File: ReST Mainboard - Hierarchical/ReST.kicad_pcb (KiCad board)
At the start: 2 copper layers, 100 x 100 mm, 164 parts, among them IC1 AT24C256, P1 CONN_01X02, P10 CONN_02X04, P11 CONN_01X04, P12 CONN_01X04, P13 CONN_01X04, P14 CONN_01X04, P15 USB_OTG, P16 CONN_02X05, P17 CONN_02X05, P18 CONN_02X05, P19 CONN_01X04, P2 CONN_01X03, P20 CONN_01X02, P21 CONN_01X04, P22 CONN_02X03, P23 CONN_02X03, P24 CONN_01X04, P25 CONN_02X03, P26 CONN_02X03, P27 CONN_02X06, P28 CONN_02X02, P29 CONN_01X02, P3 CONN_01X02, P30 CONN_01X02, P31 CONN_01X02, P32 CONN_02X02, P33 CONN_02X02, P34 CONN_02X02, P35 CONN_02X03, P36 CONN_02X03, P37 CONN_02X03, P38 CONN_02X03, P39 CONN_02X03, P4 CONN_01X03, P5 CONN_01X03, P6 CONN_01X03, P7 CONN_01X03, P8 CONN_01X03, P9 CONN_01X03, Q1 TBD, Q10 Q_AOT240L, Q11 Q_AOT240L, Q12 Q_AOT240L, Q2 TBD, Q3 TBD, Q4 TBD, Q7 Q_BSH105/IRLML2502, Q8 Q_BSH105/IRLML2502, Q9 Q_BSH105/IRLML2502, U10 USBLC6-2, U3 ACT4088, U4 SC4626, U9 STM32F1/STM32F4, X1 Crystal_Small

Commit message: removed copper and solder mask around screw holes
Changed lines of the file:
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@@
 (kicad_pcb (version 4) (host pcbnew 4.0.2-stable)
   (general
-    (links 0)
+    (links 456)
     (no_connects 0)
-    (area 18.45 61.641666 122.348 168.25)
+    (area 19.444999 65.444999 119.455001 165.455001)
     (thickness 1.6)
     (drawings 1437)
@@
   )
   (layers
-    (0 F.Cu signal hide)
-    (31 B.Cu signal hide)
+    (0 F.Cu signal)
+    (31 B.Cu signal)
     (32 B.Adhes user)
     (33 F.Adhes user)
@@
     (mod_text_size 0.75 0.75)
     (mod_text_width 0.1)
-    (pad_size 1.6 1.6)
-    (pad_drill 0)
+    (pad_size 3.2 3.2)
+    (pad_drill 3.2)
     (pad_to_mask_clearance 0)
     (aux_axis_origin 246.2 149.45)
     (grid_origin 104.45 160.45)
-    (visible_elements 7FFFFDFF)
+    (visible_elements 7FFFFFFF)
     (pcbplotparams
       (layerselection 0x010f0_80000001)
@@
     (add_net "/Stepper and Endstop/Z_2B")
   )
+  (module ReST-Library:1pin locked (layer F.Cu)
+    (at 114.45 70.45)
+    (descr "module 1 pin (ou trou mecanique de percage)")
+    (tags DEV)
+    (solder_mask_margin 1.3)
+    (clearance 1.3)
+    (fp_text reference REF** (at 0 -0.9) (layer F.Fab)
+      (effects (font (size 1 1) (thickness 0.15)))
+    )
+    (fp_text value 1pin (at 0 1.2) (layer F.Fab)
+      (effects (font (size 1 1) (thickness 0.15)))
+    )
+    (pad "" thru_hole circle (at 0 0) (size 3.2 3.2) (drill 3.2) (layers *.Cu *.Mask F.SilkS))
+  )
+  (module ReST-Library:1pin locked (layer F.Cu)
+    (at 114.45 160.45)
+    (descr "module 1 pin (ou trou mecanique de percage)")
+    (tags DEV)
+    (solder_mask_margin 1.3)
+    (clearance 1.3)
+    (fp_text reference REF** (at 0 -0.9) (layer F.Fab)
+      (effects (font (size 1 1) (thickness 0.15)))
+    )
+    (fp_text value 1pin (at 0 1.2) (layer F.Fab)
+      (effects (font (size 1 1) (thickness 0.15)))
+    )
+    (pad "" thru_hole circle (at 0 0) (size 3.2 3.2) (drill 3.2) (layers *.Cu *.Mask F.SilkS))
+  )
+  (module ReST-Library:1pin locked (layer F.Cu)
+    (at 24.45 160.45)
+    (descr "module 1 pin (ou trou mecanique de percage)")
+    (tags DEV)
+    (solder_mask_margin 1.3)
+    (clearance 1.3)
+    (fp_text reference REF** (at 0 -0.9) (layer F.Fab)
+      (effects (font (size 1 1) (thickness 0.15)))
+    )
+    (fp_text value 1pin (at 0 1.2) (layer F.Fab)
+      (effects (font (size 1 1) (thickness 0.15)))
+    )
+    (pad "" thru_hole circle (at 0 0) (size 3.2 3.2) (drill 3.2) (layers *.Cu *.Mask F.SilkS))
+  )
   (module ReST-Library:DO-214AC.SMA (layer F.Cu)
     (at 56.75 144.15)
@@
   )
   (module ReST-Library:1pin locked (layer F.Cu)
-    (at 24.45 160.45)
-    (descr "module 1 pin (ou trou mecanique de percage)")
-    (tags DEV)
-    (fp_text reference REF** (at 0 -0.9) (layer F.Fab)
-      (effects (font (size 1 1) (thickness 0.15)))
-    )
-    (fp_text value 1pin (at 0 1.2) (layer F.Fab)
-      (effects (font (size 1 1) (thickness 0.15)))
-    )
-    (pad "" np_thru_hole circle (at 0 0) (size 5.8 5.8) (drill 3.2) (layers *.Cu *.Mask F.SilkS))
-  )
-  (module ReST-Library:1pin locked (layer F.Cu)
-    (at 114.45 160.45)
-    (descr "module 1 pin (ou trou mecanique de percage)")
-    (tags DEV)
-    (fp_text reference REF** (at 0 -0.9) (layer F.Fab)
-      (effects (font (size 1 1) (thickness 0.15)))
-    )
-    (fp_text value 1pin (at 0 1.2) (layer F.Fab)
-      (effects (font (size 1 1) (thickness 0.15)))
-    )
-    (pad "" np_thru_hole circle (at 0 0) (size 5.8 5.8) (drill 3.2) (layers *.Cu *.Mask F.SilkS))
-  )
-  (module ReST-Library:1pin locked (layer F.Cu)
-    (at 114.45 70.45)
-    (descr "module 1 pin (ou trou mecanique de percage)")
-    (tags DEV)
-    (fp_text reference REF** (at 0 -0.9) (layer F.SilkS)
-      (effects (font (size 1 1) (thickness 0.15)))
-    )
-    (fp_text value 1pin (at 0 1.2) (layer F.Fab)
-      (effects (font (size 1 1) (thickness 0.15)))
-    )
-    (pad "" np_thru_hole circle (at 0 0) (size 5.8 5.8) (drill 3.2) (layers *.Cu *.Mask F.SilkS))
-  )
-  (module ReST-Library:1pin locked (layer F.Cu)
     (at 24.45 70.45)
     (descr "module 1 pin (ou trou mecanique de percage)")
     (tags DEV)
+    (solder_mask_margin 1.3)
+    (clearance 1.3)
     (fp_text reference REF** (at 0 -0.9) (layer F.Fab)
       (effects (font (size 1 1) (thickness 0.15)))
@@
       (effects (font (size 1 1) (thickness 0.15)))
     )
-    (pad "" np_thru_hole circle (at 0 0) (size 5.8 5.8) (drill 3.2) (layers *.Cu *.Mask F.SilkS))
+    (pad "" thru_hole circle (at 0 0) (size 3.2 3.2) (drill 3.2) (layers *.Cu *.Mask F.SilkS))
   )
   (module Capacitors_SMD:C_0805_HandSoldering (layer F.Cu)
@@
     (effects (font (size 1 1) (thickness 0.25)) (justify mirror))
   )
-  (gr_text "Y Min" (at 108.45 75.75 360) (layer B.SilkS)
+  (gr_text "Y Min" (at 108.45 75.75) (layer B.SilkS)
     (effects (font (size 1 1) (thickness 0.25)) (justify mirror))
   )

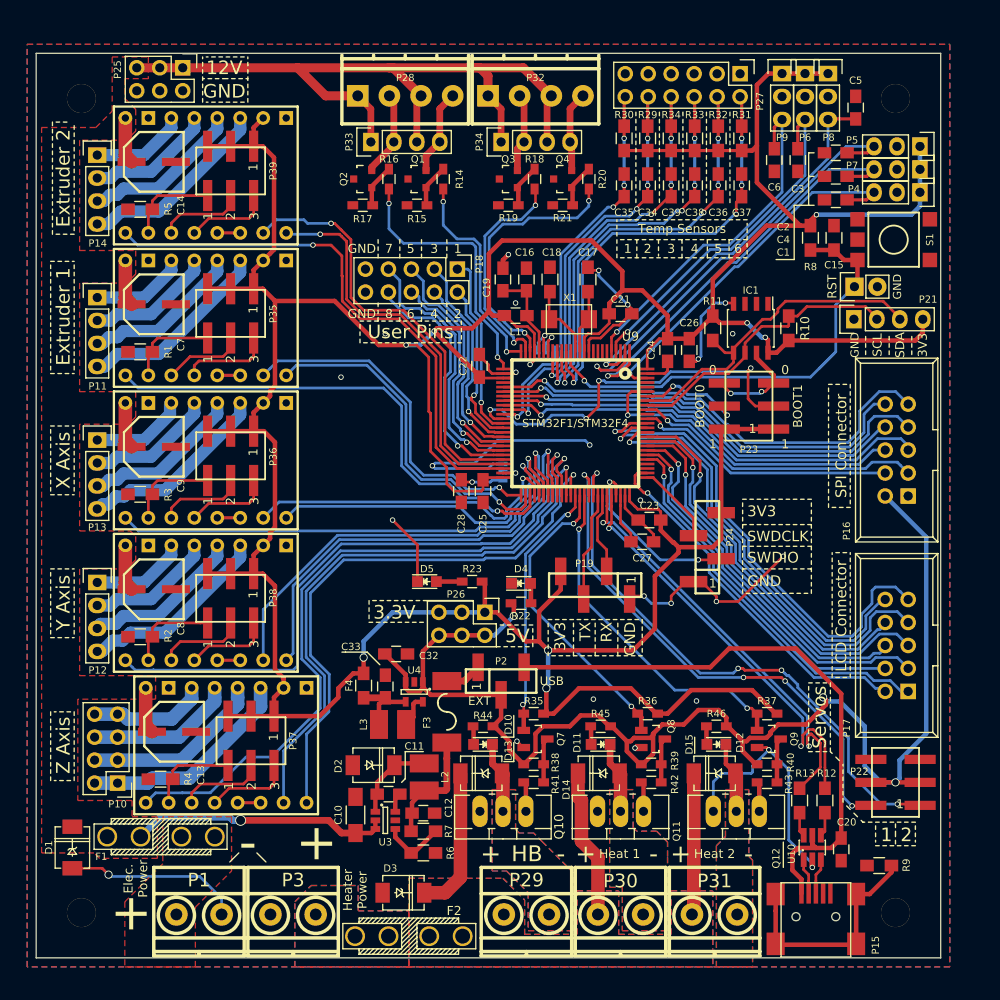
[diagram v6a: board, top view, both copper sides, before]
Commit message: Added ESP To the Mainboard
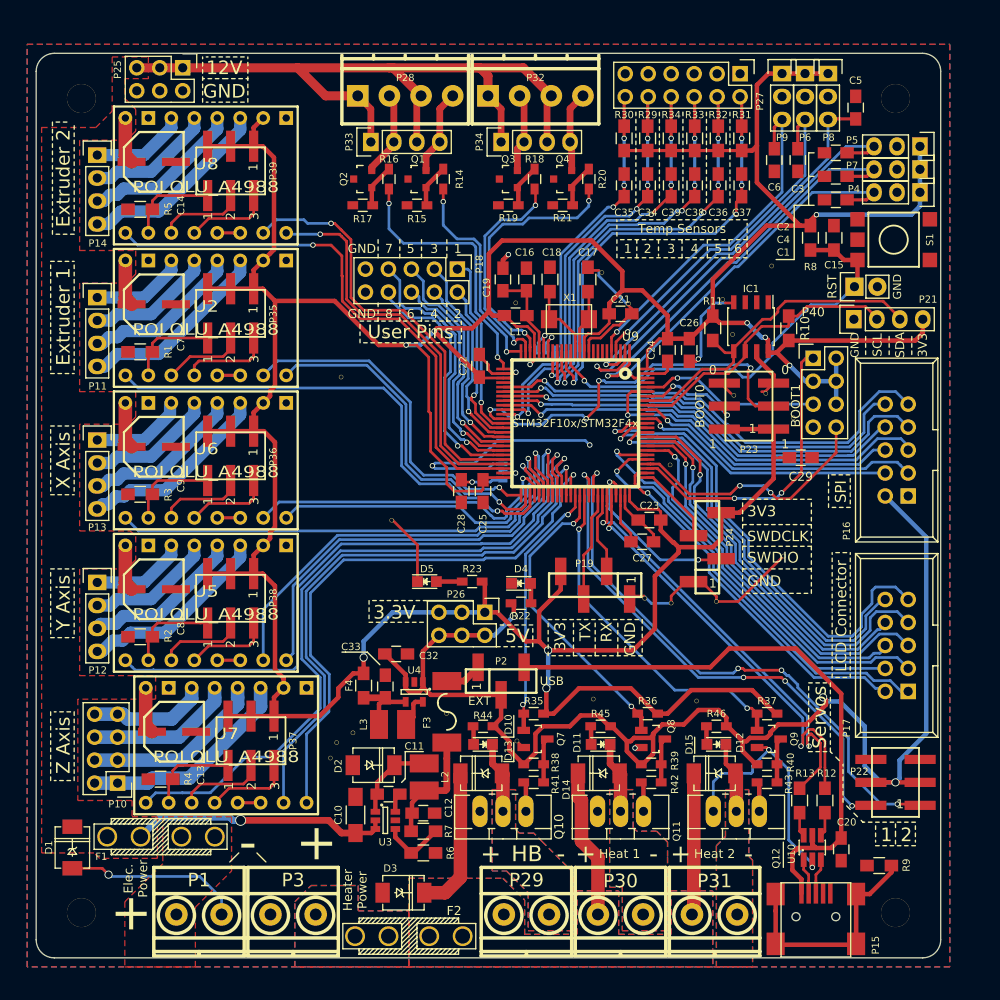
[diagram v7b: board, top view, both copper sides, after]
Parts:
- removed ? (x5): POLOLU_A4988, ReST-Library:SWDIP8_.6W
- added C29: 100nF, Capacitors_SMD:C_0805_HandSoldering, F.Cu at (104.0, 110.2)
- added P40: CONN_02X04, Pin_Headers:Pin_Header_Straight_2x04, F.Cu at (105.3, 99.2)
- added REF**: 1pin, ReST-Library:1pin, F.Cu at (86.7, 125.7)
- added REF**: 1pin, ReST-Library:1pin, F.Cu at (89.5, 111.0)
- added REF**: 1pin, ReST-Library:1pin, F.Cu at (100.8, 89.0)
- added REF**: 1pin, ReST-Library:1pin, F.Cu at (53.2, 101.2)
- added REF**: 1pin, ReST-Library:1pin, F.Cu at (58.8, 117.1)
- added REF**: 1pin, ReST-Library:1pin, F.Cu at (72.6, 141.5)
- added REF**: 1pin, ReST-Library:1pin, F.Cu at (52.0, 143.4)
- added REF**: 1pin, ReST-Library:1pin, F.Cu at (52.7, 141.7)
- added REF**: 1pin, ReST-Library:1pin, F.Cu at (54.5, 140.6)
- added REF**: 1pin, ReST-Library:1pin, F.Cu at (64.8, 138.4)
- added REF**: 1pin, ReST-Library:1pin, F.Cu at (92.5, 137.1)
- added REF**: 1pin, ReST-Library:1pin, F.Cu at (100.1, 103.0)
- added REF**: 1pin, ReST-Library:1pin, F.Cu at (81.0, 136.8)
- added REF**: 1pin, ReST-Library:1pin, F.Cu at (89.7, 126.2)
- added REF**: 1pin, ReST-Library:1pin, F.Cu at (94.7, 126.0)
- added REF**: 1pin, ReST-Library:1pin, F.Cu at (102.1, 121.0)
- added REF**: 1pin, ReST-Library:1pin, F.Cu at (103.2, 105.8)
- added REF**: 1pin, ReST-Library:1pin, F.Cu at (96.6, 103.3)
- added REF**: 1pin, ReST-Library:1pin, F.Cu at (96.4, 96.5)
- added REF**: 1pin, ReST-Library:1pin, F.Cu at (95.3, 92.7)
- added REF**: 1pin, ReST-Library:1pin, F.Cu at (84.9, 93.1)
- added REF**: 1pin, ReST-Library:1pin, F.Cu at (82.0, 89.7)
- added REF**: 1pin, ReST-Library:1pin, F.Cu at (72.5, 93.0)
- added REF**: 1pin, ReST-Library:1pin, F.Cu at (58.1, 96.5)
- added U2: POLOLU_A4988, ReST-Library:SWDIP8_.6W, F.Cu at (38.2, 94.7)
- added U5: POLOLU_A4988, ReST-Library:SWDIP8_.6W, F.Cu at (38.2, 126.2)
- added U6: POLOLU_A4988, ReST-Library:SWDIP8_.6W, F.Cu at (38.2, 110.5)
- added U7: POLOLU_A4988, ReST-Library:SWDIP8_.6W, F.Cu at (40.5, 141.9)
- added U8: POLOLU_A4988, ReST-Library:SWDIP8_.6W, F.Cu at (38.2, 79.0)
- U9: value STM32F1/STM32F4 -> STM32F10x/STM32F4x
- moved IC1 0.18 mm to (98.5, 95.7)
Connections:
- U9 pad 78: (no net) -> UART_4_TX
- U9 pad 79: (no net) -> UART_4_RX
- U9 pad 96: (no net) -> DISPLAY_EXTRA_1
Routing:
- net UART_4_TX: track 0.00 -> 33.6 mm, vias 0 -> 2
- net UART_4_RX: track 0.00 -> 28.2 mm, vias 0 -> 2
- net DISPLAY_EXTRA_1: track 0.00 -> 20.3 mm, vias 0 -> 1
- net +3V3: track 483.3 -> 502.0 mm, vias 9 -> 10
- net DISPLAY_D0: track 39.9 -> 44.8 mm
- net DISPLAY_CS: track 43.0 -> 47.9 mm
- net RESET: track 52.7 -> 48.9 mm
- net GND: track 164.0 -> 160.5 mm, vias 21 -> 10
- net (no net): vias 7 -> 0
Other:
- outline, holes or cut-outs redrawn
- board text added: "SPI"
- board text removed: "SPI Connector"
